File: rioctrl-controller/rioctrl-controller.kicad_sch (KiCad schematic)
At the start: 0 parts

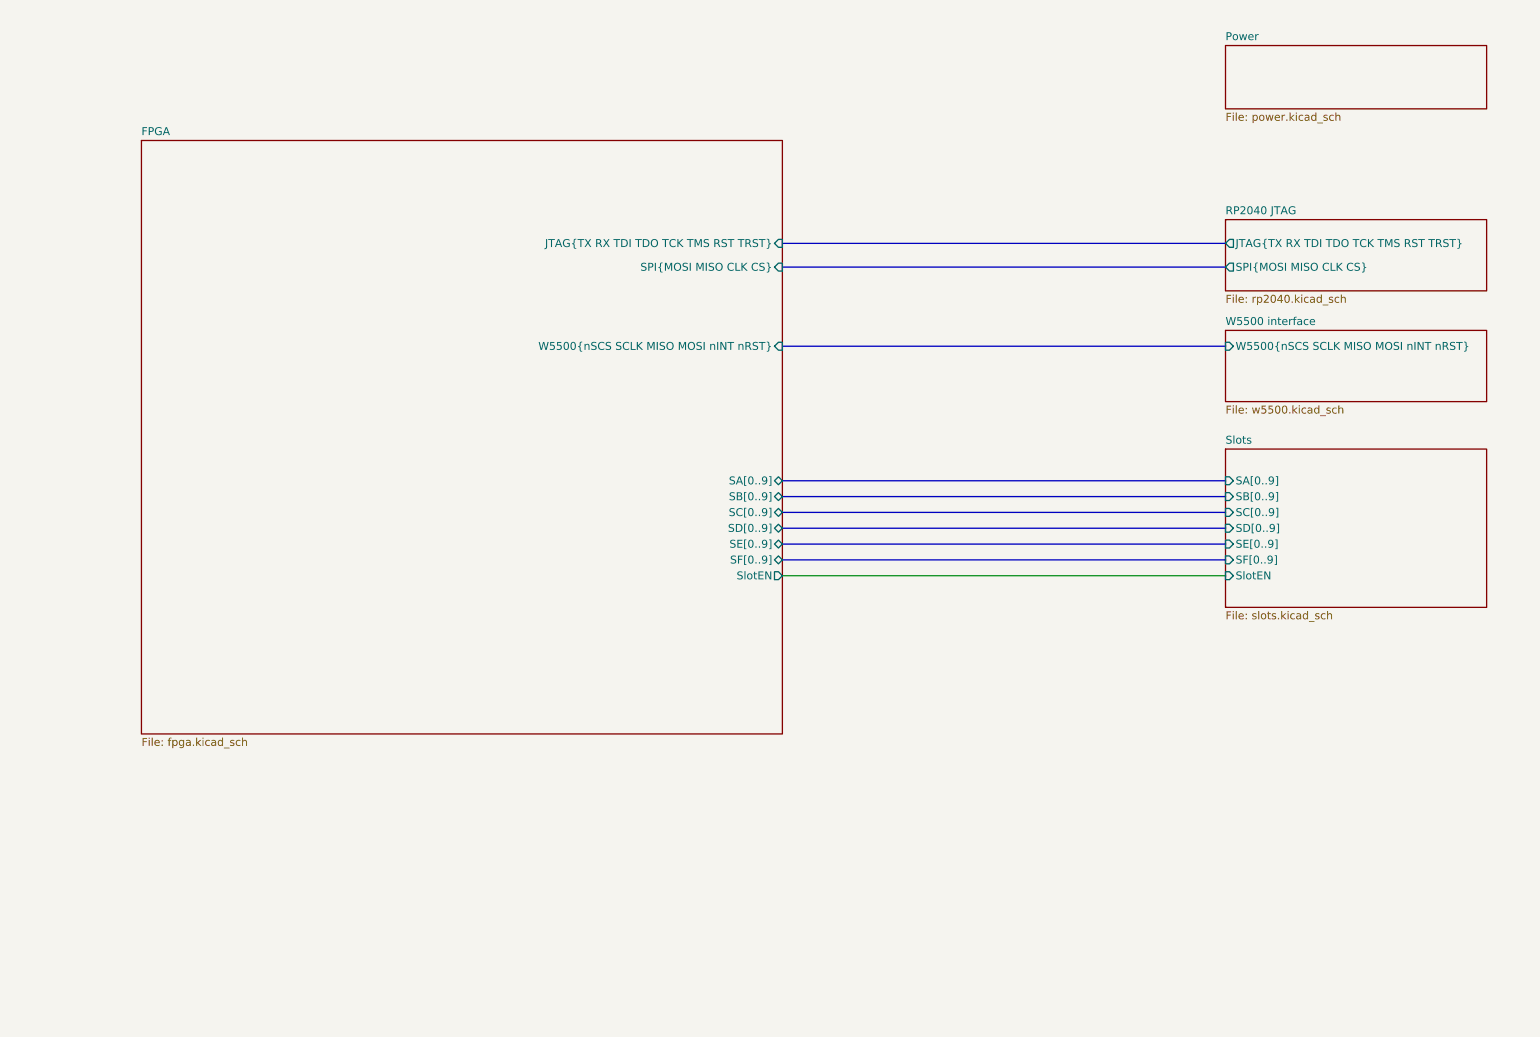
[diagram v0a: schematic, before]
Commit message: Ditch the separate backplane board, increase the slot bitwidth to 12
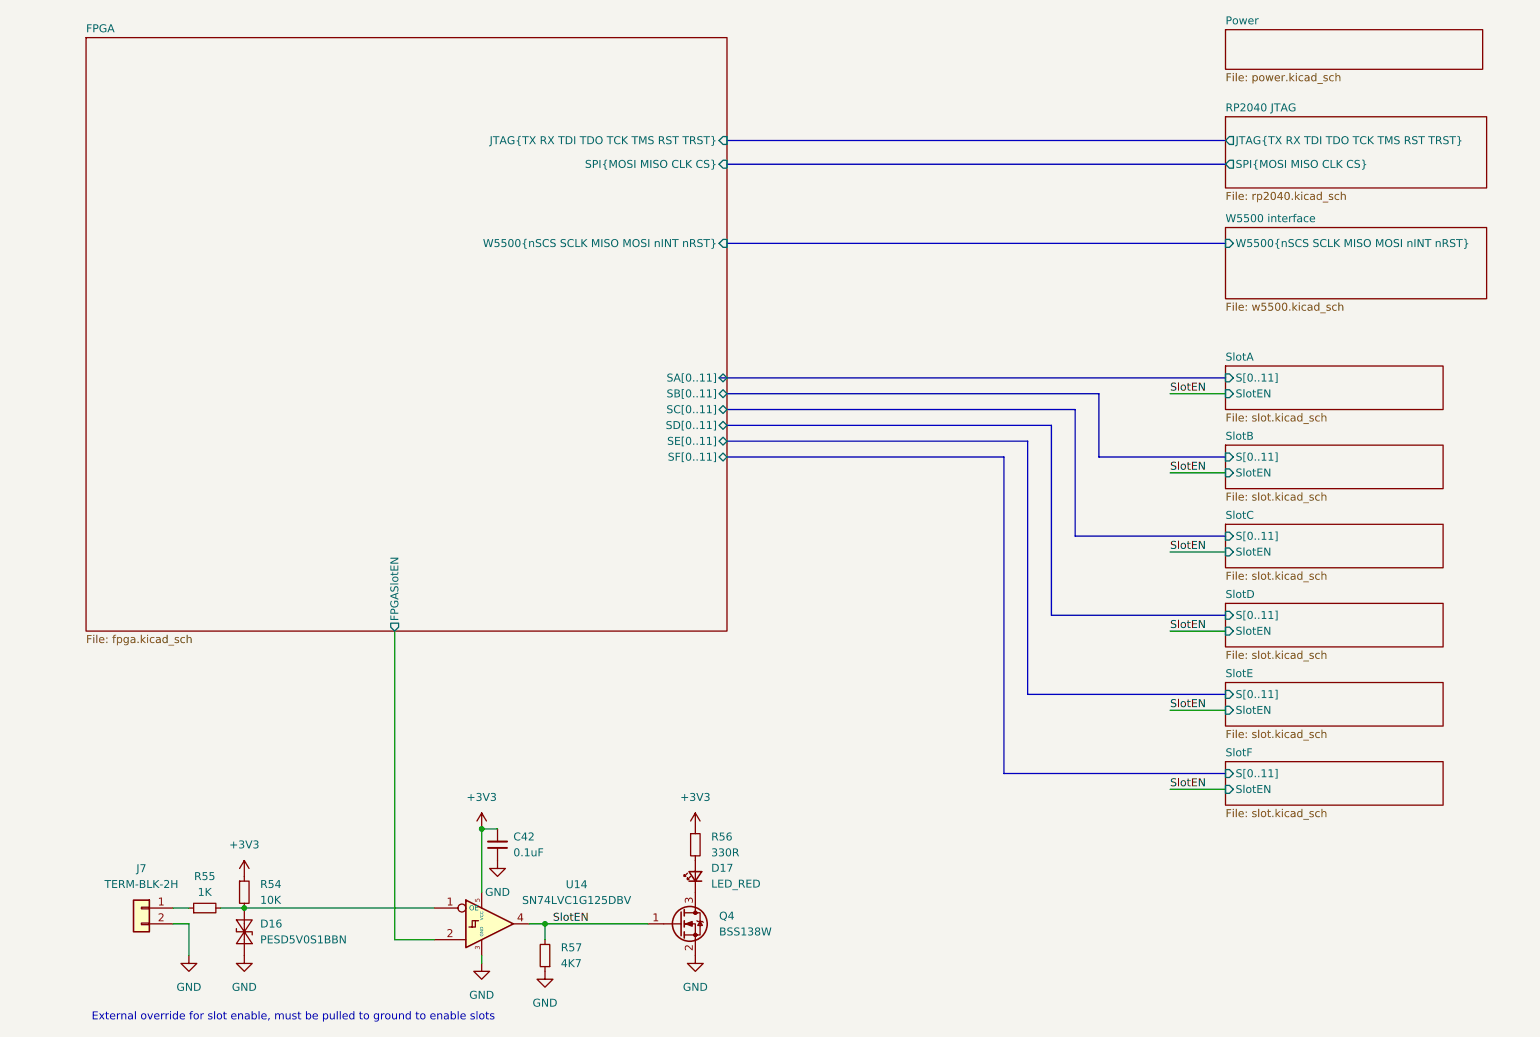
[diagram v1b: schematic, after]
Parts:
- added C42: 0.1uF, Capacitor_SMD:C_0603_1608Metric, symbol Device:C_Small
- added D16: PESD5V0S1BBN, Diode_SMD:D_SOD-523, symbol hadv-protection:PESD5V0S1BBN
- added D17: LED_RED, LED_SMD:LED_0603_1608Metric, symbol hadv-ui:LED_RED
- added J7: TERM-BLK-2H, Connector_Phoenix_MC:PhoenixContact_MC_1,5_2-G-3.5_1x02_P3.50mm_Horizontal, symbol hadv-connectors:TERM-BLK-2H
- added Q4: BSS138W, Package_TO_SOT_SMD:SOT-323_SC-70, symbol hadv-transistors:BSS138W
- added R54: 10K, Resistor_SMD:R_0603_1608Metric, symbol Device:R_Small
- added R55: 1K, Resistor_SMD:R_0603_1608Metric, symbol Device:R_Small
- added R56: 330R, Resistor_SMD:R_0603_1608Metric, symbol Device:R_Small
- added R57: 4K7, Resistor_SMD:R_0603_1608Metric, symbol Device:R_Small
- added U14: SN74LVC1G125DBV, Package_TO_SOT_SMD:SOT-23-5, symbol hadv-buffers-translators:SN74LVC1G125DBV
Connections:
- new net: D17.2 (A), R56.2
- new net: D16.2 (A2), R54.2, R55.2, U14.1 (OE)
- new net: D17.1 (K), Q4.3 (D)
- new net: J7.1 (Pin_1), R55.1
- new net +3V3: C42.2, R54.1, R56.1, U14.5 (VCC)
- new net FPGA/FPGASlotEN: U14.2
- new net GND: C42.1, D16.1 (A1), J7.2 (Pin_2), Q4.2 (S), R57.1, U14.3 (GND)
- new net SlotEN: Q4.1 (G), R57.2, U14.4
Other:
- removed sheet Slots
- added sheet SlotA (slot.kicad_sch)
- added sheet SlotB (slot.kicad_sch)
- added sheet SlotC (slot.kicad_sch)
- added sheet SlotD (slot.kicad_sch)
- added sheet SlotE (slot.kicad_sch)
- added sheet SlotF (slot.kicad_sch)
- sheet FPGA ports: added FPGASlotEN, SA[0..11], SB[0..11], SC[0..11], SD[0..11], SE[0..11], SF[0..11]; removed SA[0..9], SB[0..9], SC[0..9], SD[0..9], SE[0..9], SF[0..9], SlotEN
- note added: "External override for slot enable, must be pulled to ground to enable slots"

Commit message: Fix ERC, add title information to sch, add initial version of build scripts
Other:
- company: (none) -> R. Veips
- title: (none) -> ${PROJECTNAME}
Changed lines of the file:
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@@
 	(generator_version "8.0")
 	(paper "A4")
+	(title_block
+		(title "${PROJECTNAME}")
+		(date "2024-08-25")
+		(rev "${VERSION}")
+		(company "R. Veips")
+	)
 	(junction
 		(at 121.92 143.51)

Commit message: Fill in BOM (LCSC#)
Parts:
- C42: LCSC# (none) -> C14663
- R54: LCSC# (none) -> C98220
- R55: LCSC# (none) -> C22548
- R56: LCSC# (none) -> C105881
- R57: LCSC# (none) -> C99782
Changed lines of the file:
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@@
+			)
+		)
+		(property "LCSC#" "C105881"
+			(at 156.21 146.05 0)
+			(effects
+				(font
+					(size 1.27 1.27)
+				)
+				(hide yes)
 			)
 		)
@@
 			)
 		)
+		(property "LCSC#" "C99782"
+			(at 132.08 163.83 0)
+			(effects
+				(font
+					(size 1.27 1.27)
+				)
+				(hide yes)
+			)
+		)
 		(pin "1"
 		)
@@
 			)
 		)
+		(property "LCSC#" "C14663"
+			(at 124.46 146.05 0)
+			(effects
+				(font
+					(size 1.27 1.27)
+				)
+				(hide yes)
+			)
+		)
 		(pin "1"
 		)
@@
 			)
 		)
+		(property "LCSC#" "C98220"
+			(at 83.82 153.67 0)
+			(effects
+				(font
+					(size 1.27 1.27)
+				)
+				(hide yes)
+			)
+		)
 		(pin "1"
 		)
@@
 			(at 77.47 156.21 0)
 			(effects
+				(font
+					(size 1.27 1.27)
+				)
+				(hide yes)
+			)
+		)
+		(property "LCSC#" "C22548"
+			(at 77.47 156.21 0)
+			(effects

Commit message: Add pulldown for SlotEN signal
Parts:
- added R63: 4K7, Resistor_SMD:R_0603_1608Metric, symbol Device:R_Small
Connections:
- net FPGA/FPGASlotEN: now also R63.2
- net GND: now also R63.1
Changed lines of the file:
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@@
+	)
+	(junction
+		(at 107.95 161.29)
+		(diameter 0)
+		(color 0 0 0 0)
 	)
 	(junction
@@
 	(symbol
 		(lib_id "power:GND")
+		(at 107.95 166.37 0)
+		(unit 1)
+		(exclude_from_sim no)
+		(in_bom yes)
+		(on_board yes)
+		(dnp no)
+		(fields_autoplaced yes)
+		(property "Reference" "#PWR0220"
+			(at 107.95 172.72 0)
+			(effects
+				(font
+					(size 1.27 1.27)
+				)
+				(hide yes)
+			)
+		)
+		(property "Value" "GND"
+			(at 107.95 171.45 0)
+			(effects
+				(font
+					(size 1.27 1.27)
+				)
+			)
+		)
+		(property "Footprint" ""
+			(at 107.95 166.37 0)
+			(effects
+				(font
+					(size 1.27 1.27)
+				)
+				(hide yes)
+			)
+		)
+		(property "Datasheet" ""
+			(at 107.95 166.37 0)
+			(effects
+				(font
+					(size 1.27 1.27)
+				)
+				(hide yes)
+			)
+		)
+		(property "Description" "Power symbol creates a global label with name \"GND\" , ground"
+			(at 107.95 166.37 0)
+			(effects
+				(font
+					(size 1.27 1.27)
+				)
+				(hide yes)
+			)
+		)
+		(pin "1"
+		)
+		(instances
+			(project "rioctrl-controller"
+				(path "/41b9ee15-835e-4b63-93e8-ca4d10e95680"
+					(reference "#PWR0220")
+					(unit 1)
+				)
+			)
+		)
+	)
+	(symbol
+		(lib_id "power:GND")
 		(at 132.08 166.37 0)
 		(unit 1)
@@
 					(unit 1)
 				)
+			)
+		)
+	)
+	(symbol
+		(lib_id "Device:R_Small")
+		(at 107.95 163.83 180)
+		(unit 1)
+		(exclude_from_sim no)
+		(in_bom yes)
+		(on_board yes)
+		(dnp no)
+		(fields_autoplaced yes)
+		(property "Reference" "R63"
+			(at 110.49 162.5599 0)
+			(effects
+				(font
+					(size 1.27 1.27)
+				)
+				(justify right)
+			)
+		)
+		(property "Value" "4K7"
+			(at 110.49 165.0999 0)
+			(effects
+				(font
+					(size 1.27 1.27)
+				)
+				(justify right)
+			)
+		)
+		(property "Footprint" "Resistor_SMD:R_0603_1608Metric"
+			(at 107.95 163.83 0)
+			(effects
+				(font
+					(size 1.27 1.27)
+				)
+				(hide yes)
+			)
+		)
+		(property "Datasheet" "~"
+			(at 107.95 163.83 0)
+			(effects
+				(font
+					(size 1.27 1.27)
+				)
+				(hide yes)
+			)
+		)
+		(property "Description" "Resistor, small symbol"
+			(at 107.95 163.83 0)
+			(effects
+				(font
+					(size 1.27 1.27)
+				)
+				(hide yes)
+			)
+		)
+		(property "LCSC#" "C99782"
+			(at 107.95 163.83 0)
+			(effects
+				(font
+					(size 1.27 1.27)
+				)
+				(hide yes)
+			)
+		)
+		(pin "1"
+		)
+		(pin "2"
+		)
+		(instances
+			(project "rioctrl-controller"
+				(path "/41b9ee15-835e-4b63-93e8-ca4d10e95680"
+					(reference "R63")
+					(unit 1)
+				)
